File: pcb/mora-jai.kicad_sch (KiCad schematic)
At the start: 28 parts, among them J1 Conn_01x02, J2 Conn_01x04, J3 Conn_01x02, J4 Conn_01x01, J5 Conn_01x03, SW1 SW_Push, SW10 SW_Push, SW11 SW_Push, SW12 SW_Push, SW13 SW_Push, SW14 SW_Push, SW15 SW_Push, SW16 SW_Push, SW2 SW_Push, SW3 SW_Push, SW4 SW_Push, SW5 SW_Push, SW6 SW_Push, SW7 SW_Push, SW8 SW_Push, SW9 SW_Push, U1 CD74HC4067M, U3 XIAO-ESP32-S3-SMD

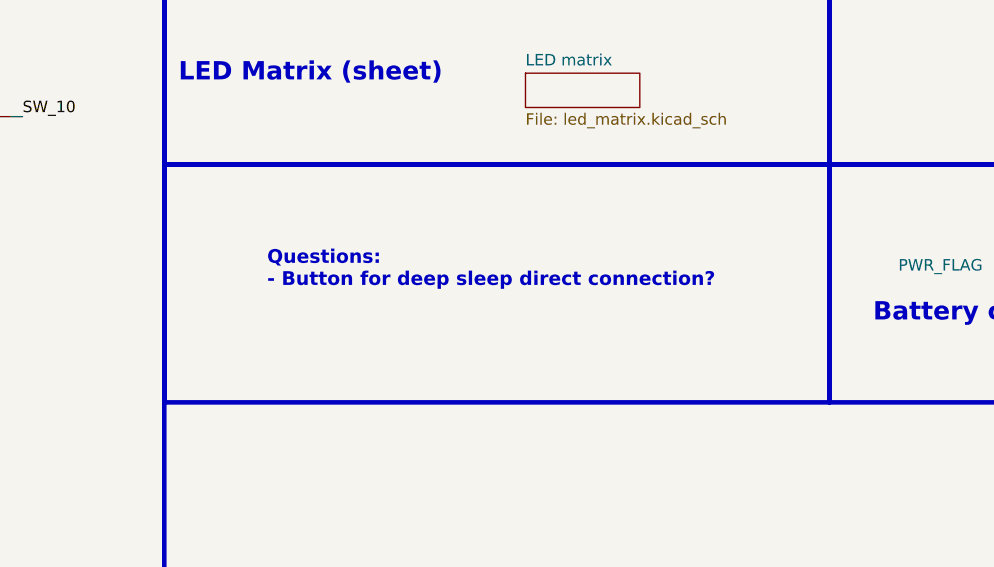
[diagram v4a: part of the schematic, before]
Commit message: clean up schematic
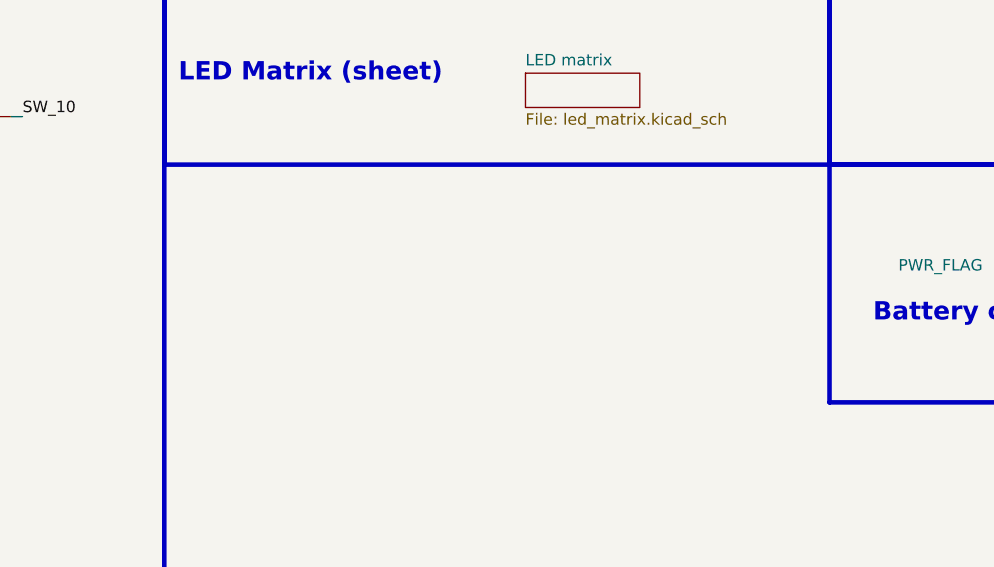
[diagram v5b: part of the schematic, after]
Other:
- note removed: "Questions: - Button for deep sleep direct connection?"
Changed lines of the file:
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@@
-	)
-	(rectangle
-		(start 132.588 103.124)
-		(end 206.502 129.54)
-		(stroke
-			(width 0.508)
-			(type solid)
-		)
-		(fill
-			(type none)
-		)
 	)
 	(rectangle
@@
 		)
 	)
-	(text "Questions:\n- Button for deep sleep direct connection?"
-		(exclude_from_sim no)
-		(at 144.018 114.808 0)
-		(effects
-			(font
-				(size 1.524 1.524)
-				(thickness 0.3048)
-				(bold yes)
-			)
-			(justify left)
-		)
-	)
